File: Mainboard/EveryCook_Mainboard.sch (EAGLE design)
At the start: 106 parts, among them IC1 LM386MM-1, IC2 ATMEGA644A, Q1 8 MHz, Q2 BSP372, Q3 BSP372, T2 ZDT6790, U1 AD7794BRUZ, U4 78M05, U7 CJ1117-3.3

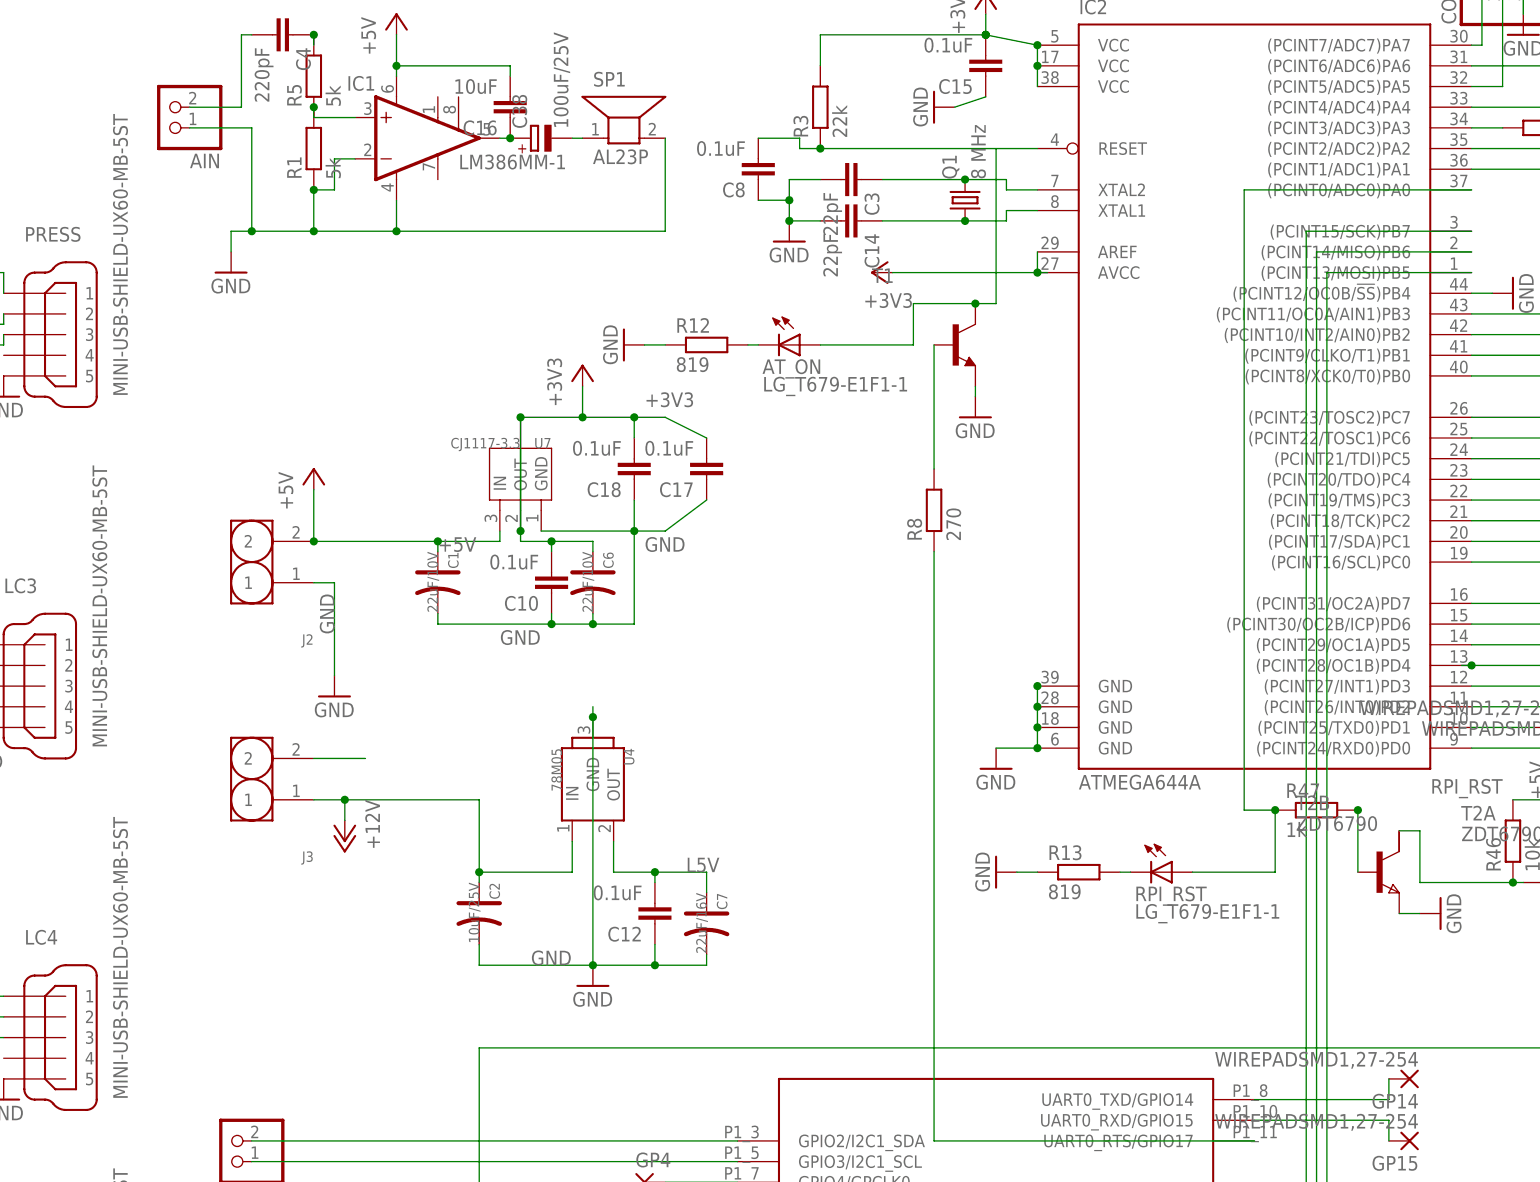
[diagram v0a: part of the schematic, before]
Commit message: Redesign of mainboard. New load cell amp board.
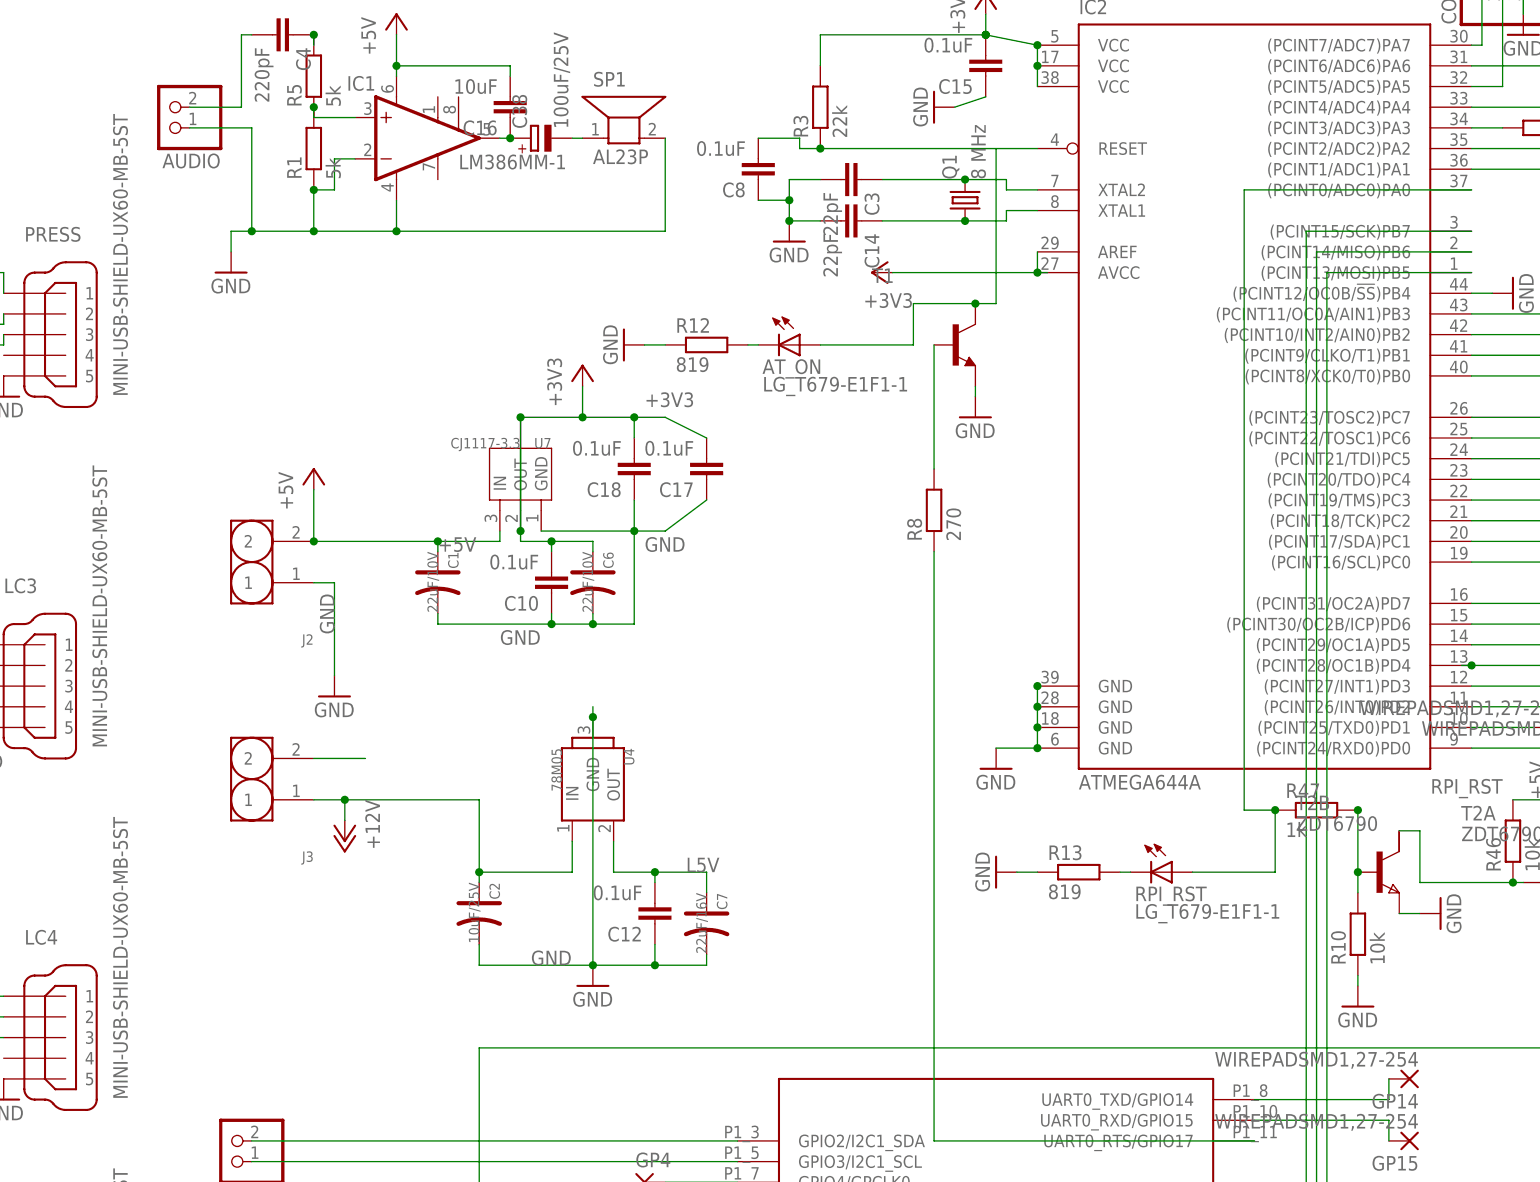
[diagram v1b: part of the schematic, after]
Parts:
- added R10: 10k, rcl:R-EU_R0805
- renumbered AIN to AUDIO
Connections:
- net GND: now also R10.1
- net N$71: now also R10.2
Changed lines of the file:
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@@
 <setting verticaltext="up"/>
 </settings>
-<grid distance="0.05" unitdist="inch" unit="inch" style="lines" multiple="1" display="no" altdistance="0.01" altunitdist="inch" altunit="inch"/>
+<grid distance="0.1" unitdist="inch" unit="inch" style="lines" multiple="1" display="no" altdistance="0.01" altunitdist="inch" altunit="inch"/>
 <layers>
 <layer number="1" name="Top" color="4" fill="1" visible="no" active="no"/>
@@
 <part name="BUT2+3" library="pinhead" deviceset="PINHD-1X3" device=""/>
 <part name="GND20" library="supply1" deviceset="GND" device=""/>
-<part name="AIN" library="pinhead" deviceset="PINHD-1X2" device=""/>
+<part name="AUDIO" library="pinhead" deviceset="PINHD-1X2" device=""/>
 <part name="U$5" library="raspberry_mirr" deviceset="RPI-B-V2" device=""/>
 <part name="T3" library="transistor" deviceset="*-NPN-" device="SOT23-BEC" technology="MMBT2222ALT1"/>
@@
 <part name="GP15" library="wirepad" deviceset="WIREPAD" device="SMD1,27-254"/>
 <part name="GP22" library="wirepad" deviceset="WIREPAD" device="SMD1,27-254"/>
+<part name="R10" library="rcl" deviceset="R-EU_" device="R0805" value="10k"/>
+<part name="GND33" library="supply1" deviceset="GND" device=""/>
 </parts>
 <sheets>
@@
 <instance part="BUT2+3" gate="A" x="149.86" y="35.56" rot="R90"/>
 <instance part="GND20" gate="1" x="138.43" y="24.13"/>
-<instance part="AIN" gate="G$1" x="-53.34" y="180.34" rot="R180"/>
+<instance part="AUDIO" gate="G$1" x="-53.34" y="180.34" rot="R180"/>
 <instance part="U$5" gate="G$1" x="41.91" y="27.94"/>
 <instance part="T3" gate="G$1" x="157.48" y="83.82"/>
@@
 <instance part="GP15" gate="G$1" x="99.06" y="53.34" rot="R180"/>
 <instance part="GP22" gate="G$1" x="99.06" y="43.18" rot="R180"/>
+<instance part="R10" gate="G$1" x="92.71" y="78.74" rot="R90"/>
+<instance part="GND33" gate="1" x="92.71" y="69.85"/>
 </instances>
 <busses>
@@
 <wire x1="7.62" y1="165.1" x2="-25.4" y2="165.1" width="0.1524" layer="91"/>
 <junction x="-25.4" y="165.1"/>
-<pinref part="AIN" gate="G$1" pin="1"/>
+<pinref part="AUDIO" gate="G$1" pin="1"/>
 <wire x1="-50.8" y1="177.8" x2="-43.18" y2="177.8" width="0.1524" layer="91"/>
 <wire x1="-43.18" y1="177.8" x2="-43.18" y2="165.1" width="0.1524" layer="91"/>
@@
 <pinref part="GND21" gate="1" pin="GND"/>
 <wire x1="160.02" y1="77.47" x2="160.02" y2="78.74" width="0.1524" layer="91"/>
+</segment>
+<segment>
+<pinref part="R10" gate="G$1" pin="1"/>
+<pinref part="GND33" gate="1" pin="GND"/>
+<wire x1="92.71" y1="73.66" x2="92.71" y2="72.39" width="0.1524" layer="91"/>
 </segment>
 </net>
@@
 <wire x1="92.71" y1="86.36" x2="92.71" y2="93.98" width="0.1524" layer="91"/>
 <junction x="92.71" y="93.98"/>
+<pinref part="R10" gate="G$1" pin="2"/>
+<wire x1="92.71" y1="86.36" x2="92.71" y2="83.82" width="0.1524" layer="91"/>
+<junction x="92.71" y="86.36"/>
 </segment>
 </net>
@@
 <wire x1="-44.45" y1="189.23" x2="-43.18" y2="189.23" width="0.1524" layer="91"/>
 <wire x1="-44.45" y1="189.23" x2="-44.45" y2="180.34" width="0.1524" layer="91"/>
-<pinref part="AIN" gate="G$1" pin="2"/>
+<pinref part="AUDIO" gate="G$1" pin="2"/>
 <wire x1="-44.45" y1="180.34" x2="-50.8" y2="180.34" width="0.1524" layer="91"/>
 </segment>
